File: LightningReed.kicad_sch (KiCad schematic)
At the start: 12 parts, among them P1 Conn_WallPlug

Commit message: PFC
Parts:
- added C10: 68uF, symbol Device:C_Polarized
- added C4: 10pF, symbol Device:C_Small
- added C5: 3900pF, symbol Device:C_Small
- added C6: 1uF, symbol Device:C_Small
- added C7: 33nF, symbol Device:C_Small
- added C8: 220pF, symbol Device:C_Small
- added C9: 2200pF, symbol Device:C_Small
- added Q1: NCE65T180D, symbol Device:Q_NMOS_GDS
- added R1: 10, symbol Device:R_Small
- added R10, R11, R12, R2, R3, R4: 3M24, symbol Device:R_Small
- added R13: 274K, symbol Device:R_Small
- added R14: 64k9, symbol Device:R_Small
- added R5: 24K3, symbol Device:R_Small
- added R6, R7: 220m, symbol Device:R_Small
- added R8: 182K, symbol Device:R_Small
- added R9: 750, symbol Device:R_Small
- added U1: UCC28056, symbol LightningReed:UCC28056
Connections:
- net GNDPWR: now also C10.2, C7.1, C8.2, C9.2, R14.1, R6.1, R7.1, R8.1, U1.4 (GND)
- net VDC: now also C10.1, R10.2
- net at D3.2 (A), L4.1: now also C4.1, Q1.2 (D), R2.2
- new net: R1.1, U1.5 (DRV)
- new net: Q1.1 (G), R1.2
- new net: R3.1, R4.2
- new net: R2.1, R3.2
- new net: C5.2, Q1.3 (S), R5.1, R6.2, R7.2
- new net: C4.2, C5.1, R4.1, R5.2, R9.1
- new net: R12.1, R13.2
- new net: R11.1, R12.2
- new net: C6.1, R8.2
- new net: C6.2, C7.2, U1.6 (COMP)
- new net: C9.1, R13.1, R14.2, U1.1 (VOSNS)
- new net: C8.1, R9.2, U1.2 (ZCD)
- new net: R10.1, R11.2
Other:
- note added: "EWH2WM680M20OT"

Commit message: brown out circuit
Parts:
- added C11, C12, C13: 1uF, symbol Device:C_Small
- added C14: 220pF, symbol Device:C_Small
- added Q2: 2N7002, Package_TO_SOT_SMD:SOT-23, symbol Transistor_FET:2N7002
- added R15: 2, symbol Device:R_Small
- added R16: 121K, symbol Device:R_Small
- added R17: 39K2, symbol Device:R_Small
- added R18: 100K, symbol Device:R_Small
- added U2: 78L05S, Package_TO_SOT_SMD:SOT-89-3, symbol Regulator_Linear:L78L05_SOT89
- added U3: LMC7111, symbol LightningReed:LMC7111
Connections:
- net GNDPWR: now also C11.2, C12.2, C13.2, C14.2, Q2.2 (S), R17.1, U2.2 (GND), U3.5 (V-)
- net at U1.3 (VCC): now also C11.1, R15.1
- new net: Q2.1 (G), R18.1, U3.1
- new net: R16.1, R17.2, R18.2, U3.3 (+)
- new net 5V_LDO: C13.1, R16.2, U2.1 (OUT), U3.2 (V+)
- new net AC_SENSE: C14.1, U3.4 (-)
- new net BROWN_OUT: Q2.3 (D)
- new net VCC_PFC: R15.2
- new net VDD3: C12.1, U2.3 (IN)

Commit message: PFC complete
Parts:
- added C15: 1uF, symbol Device:C_Small
- added C16, C18, C19, C20: 100nF, symbol Device:C_Small
- added C17: 33nF, symbol Device:C_Small
- added D4: BZT52C16S, symbol Device:D_Zener_Small
- added D5: DSK16, symbol Device:D_Schottky_Small
- added D6: BZT52C13, symbol Device:D_Zener_Small
- added Q3: Q_NMOS_GDS, symbol Device:Q_NMOS_GDS
- added Q4: 2N7002, Package_TO_SOT_SMD:SOT-23, symbol Transistor_FET:2N7002
- added Q5, Q6: 2N7002K, Package_TO_SOT_SMD:SOT-23, symbol Transistor_FET:2N7002K
- added R19, R20, R24: 3M24, symbol Device:R_Small
- added R21, R22, R23: 1K, symbol Device:R_Small
- added R25: 3M16, symbol Device:R_Small
- added R26: 178K, symbol Device:R_Small
- added R27, R28: 100K, symbol Device:R_Small
- added R29: 10K, symbol Device:R_Small
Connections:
- net AC_SENSE: now also R25.1, R26.2
- net BROWN_OUT: now also D4.1 (K), Q3.1 (G), Q4.1 (G), R24.1
- net GNDPWR: now also C15.2, C16.2, C17.2, C18.2, C19.2, C20.2, D4.2 (A), Q5.2 (S), Q6.2 (S), R26.1, R28.1, R29.1
- net HT: now also R19.2
- net VCC_PFC: now also C15.1, Q4.2 (S)
- net VDC: now also C18.1, C19.1, C20.1, R21.1
- net VDD3: now also D5.2 (A)
- net COMP: now reaches C6.2, C7.2, U1.6 (COMP)
- net COMP: now also Q5.3 (D)
- new net: D6.2 (A), Q6.1 (G), R29.2
- new net: D5.1 (K), Q3.3 (S), Q4.3 (D)
- new net: C16.1, R20.1, R24.2, R25.2
- new net: R22.2, R23.1
- new net: Q3.2 (D), R23.2
- new net: R21.2, R22.1
- new net: C17.1, Q5.1 (G), Q6.3 (D), R27.1, R28.2
- new net: R19.1, R20.2
- new net VDD2: D6.1 (K), R27.2

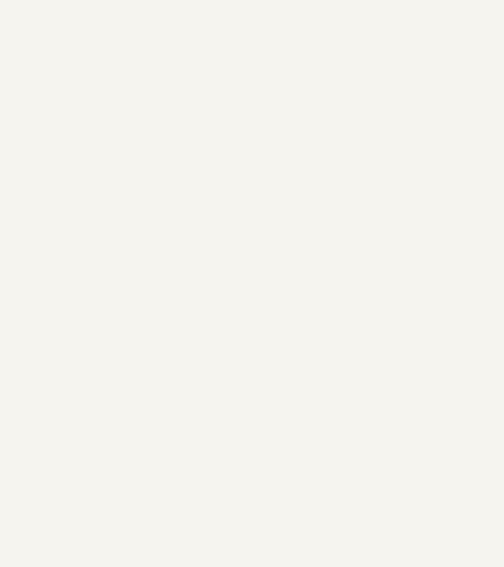
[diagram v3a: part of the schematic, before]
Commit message: Flyback controller
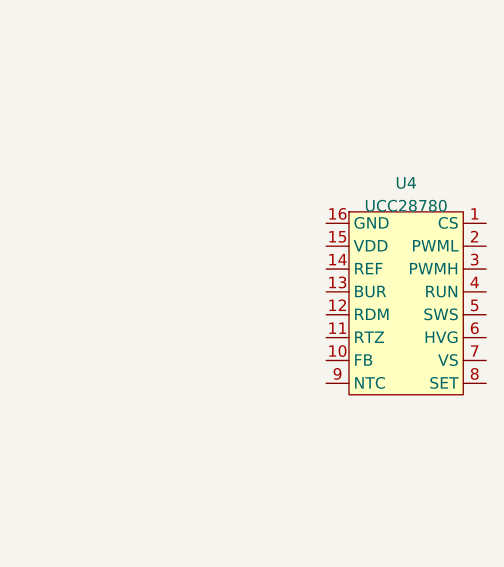
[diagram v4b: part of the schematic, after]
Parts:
- added U4: UCC28780, symbol LightningReed:UCC28780
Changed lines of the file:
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@@
+    )
+  )
+  (symbol (lib_id "LightningReed:UCC28780") (at 234.315 88.265 0) (unit 1)
+    (in_bom yes) (on_board yes) (dnp no) (fields_autoplaced)
+    (property "Reference" "U4" (at 234.315 85.09 0)
+      (effects (font (size 1.27 1.27)))
+    )
+    (property "Value" "UCC28780" (at 234.315 87.63 0)
+      (effects (font (size 1.27 1.27)))
+    )
+    (property "Footprint" "" (at 234.315 88.265 0)
+      (effects (font (size 1.27 1.27)) hide)
+    )
+    (property "Datasheet" "" (at 234.315 88.265 0)
+      (effects (font (size 1.27 1.27)) hide)
+    )
+    (pin "1")
+    (pin "10")
+    (pin "11")
+    (pin "12")
+    (pin "13")
+    (pin "14")
+    (pin "15")
+    (pin "16")
+    (pin "2")
+    (pin "3")
+    (pin "4")
+    (pin "5")
+    (pin "6")
+    (pin "7")
+    (pin "8")
+    (pin "9")
+    (instances
+      (project "LightningReed"
+        (path "/ed30a684-3009-4c45-ba04-268ec6465166"
+          (reference "U4") (unit 1)
+        )
+      )
     )
   )

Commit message: Transformer
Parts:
- added C21, C22: 330nF, symbol Device:C_Small
- added Q7, Q8: NCE65T260K, symbol Device:Q_NMOS_GDS
- added R30: 2M21, symbol Device:R_Small
- added T1: Transformer_2P_2S, symbol LightningReed:Transformer_2P_2S
- C19: value 100nF -> 470nF
- C20: value 100nF -> 330nF
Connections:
- net GNDPWR: no longer C20.2
- net VDC: now also C21.1, C22.1, R30.2, T1.2 (AB)
- new net: C20.2, C21.2, C22.2, Q7.2 (D), R30.1
- new net: Q7.3 (S), Q8.2 (D), T1.1 (AA)

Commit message: HB Driver
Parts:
- added C23: 47nF, symbol Device:C_Small
- added D7: ES1JAF, symbol Device:D_Schottky_Small
- added R31, R35: 10, symbol Device:R_Small
- added R32, R34: 10K, symbol Device:R_Small
- added R33: 24.9, symbol Device:R_Small
- added R36: 44K2, symbol Device:R_Small
- added R37: 118K, symbol Device:R_Small
- added U5: UCC27712, symbol LightningReed:UCC27712
- added U6: NCP1117-ADJ_SOT223, Package_TO_SOT_SMD:SOT-223-3_TabPin2, symbol Regulator_Linear:NCP1117-ADJ_SOT223
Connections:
- net at Q7.3 (S), Q8.2 (D), T1.1 (AA): now also C23.2, R32.2, U5.6 (HS)
- net at Q8.1 (G): now also R33.1, R34.1
- net at Q8.3 (S): now also R34.2, R37.2, U5.4 (COM)
- net at Q7.1 (G): now also R31.1, R32.1
- new net: C23.1, R35.1, U5.8 (HB)
- new net: R36.2, R37.1, U6.1 (ADJ)
- new net: D7.2 (A), R36.1, U5.3 (VDD), U6.2 (VO)
- new net: R33.2, U5.5 (LO)
- new net: R31.2, U5.7 (HO)
- new net: D7.1 (K), R35.2

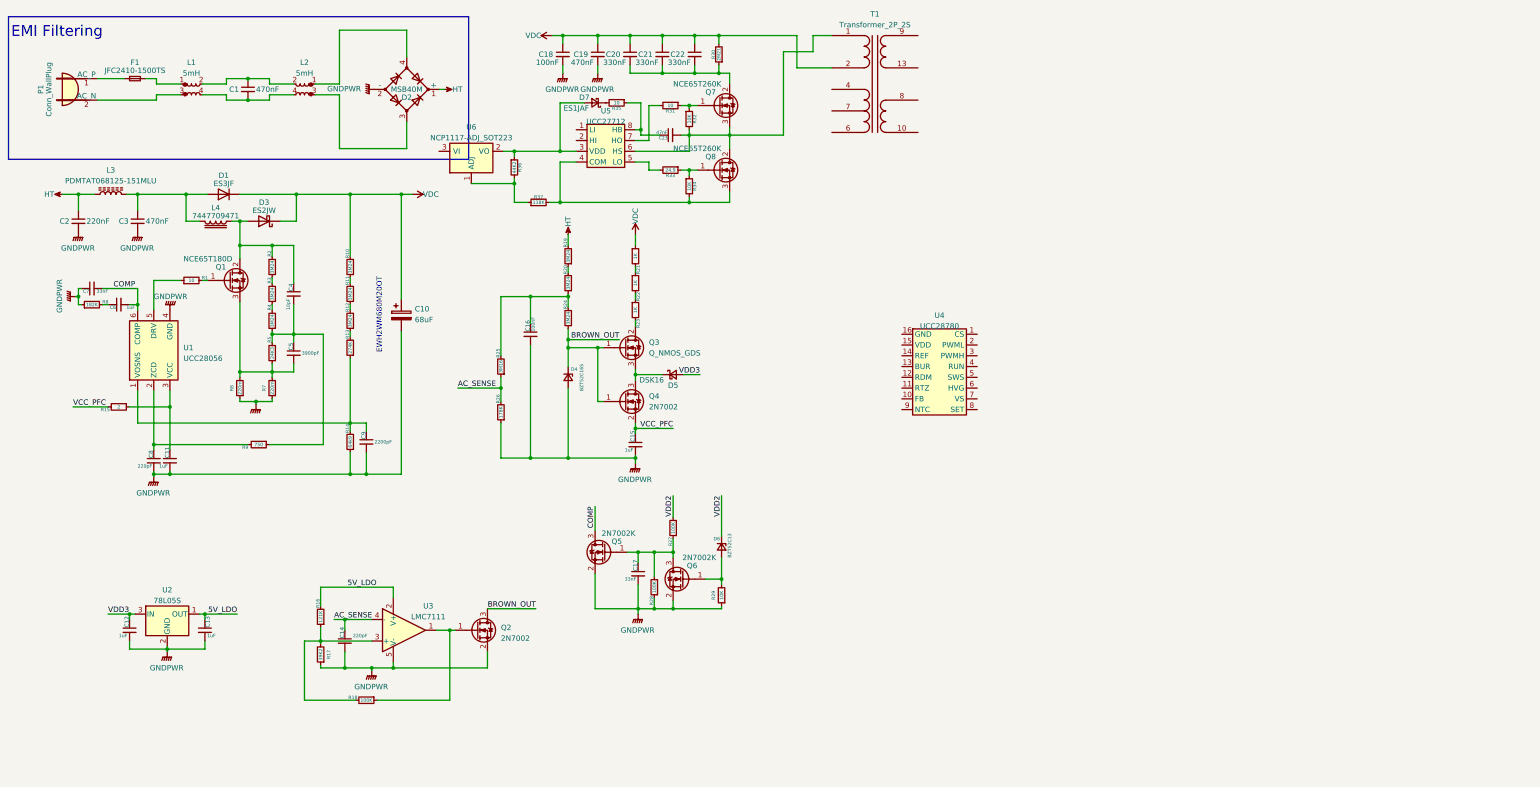
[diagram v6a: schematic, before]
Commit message: Flyback Controller VDDBias Power
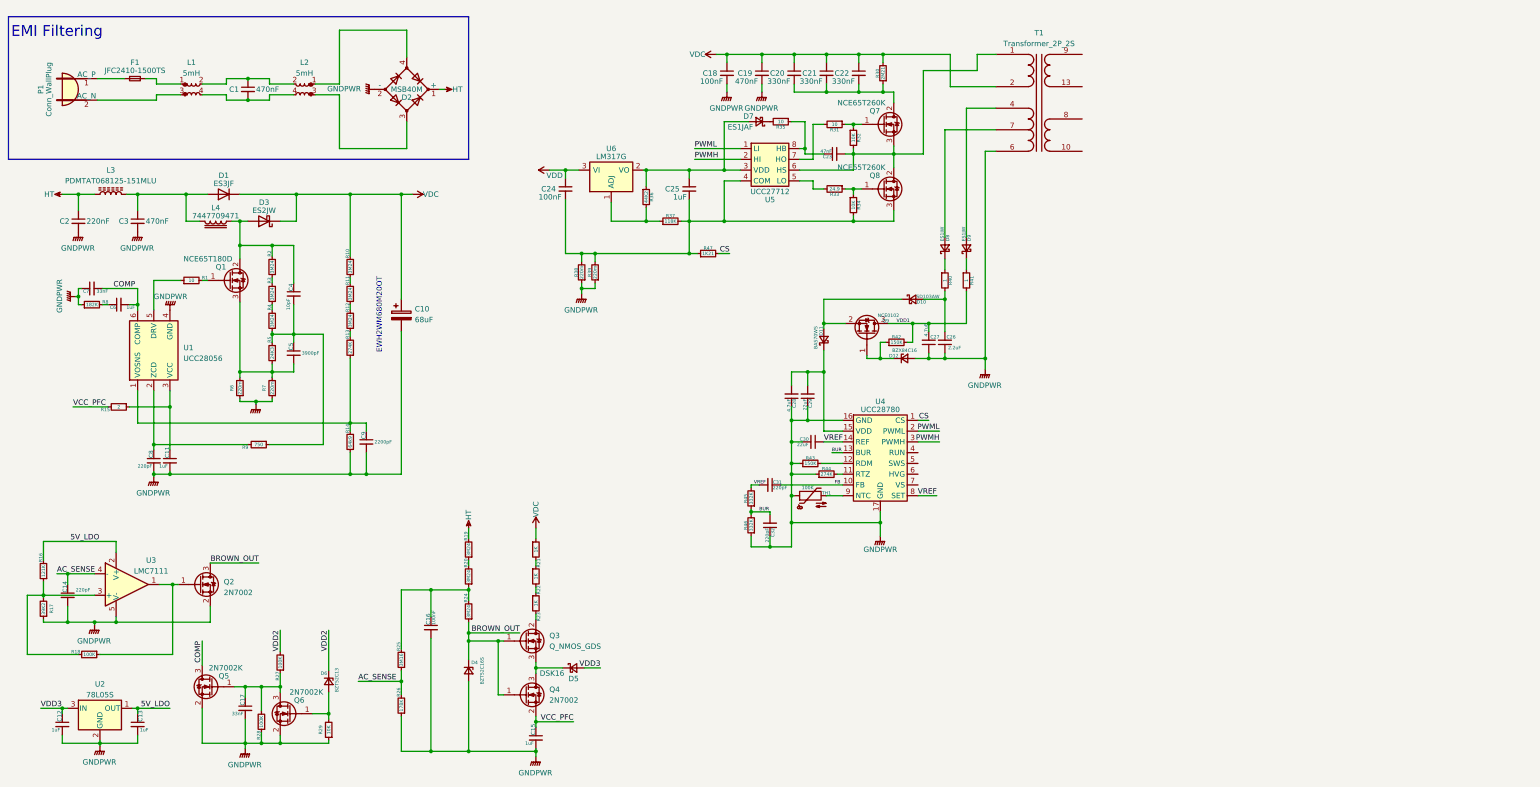
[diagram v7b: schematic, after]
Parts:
- added C24: 100nF, symbol Device:C_Small
- added C25: 1uF, symbol Device:C_Small
- added C26: 2.2uF, symbol Device:C_Small
- added C27, C28: 4.7uF, symbol Device:C_Small
- added C29, C30: 22uF, symbol Device:C_Small
- added C31, C32: 220pF, symbol Device:C_Small
- added D10: SD103AW, symbol Device:D_Schottky_Small
- added D11: BAS70WS, symbol Device:D_Schottky_Small
- added D12: BZX84C16, symbol Device:D_Zener_Small
- added D8, D9: ES1JW, symbol Device:D_Schottky_Small
- added Q9: NCE0102, symbol Device:Q_NMOS_GSD
- added R38, R39: 220m, symbol Device:R_Small
- added R40, R41: 1, symbol Device:R_Small
- added R42, R43: 150K, symbol Device:R_Small
- added R44: 274K, symbol Device:R_Small
- added R45, R46: 332K, symbol Device:R_Small
- added R47: 1K21, symbol Device:R_Small
- added TH1: 100K, symbol Device:Thermistor_NTC
- U6: value NCP1117-ADJ_SOT223 -> LM317G
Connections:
- net GNDPWR: now also T1.6 (SD), U4.16 (GND), U4.17 (GND), C26.1, C27.1, C28.1, C29.1, C30.2, C32.1, D12.2 (A), R38.1, R39.1, R43.1, R44.1, R46.1, TH1.1
- net CS: now reaches U4.1 (CS)
- net CS: now also R47.2
- net FB: now reaches U4.10 (FB)
- net FB: now also C31.1
- net at U4.11 (RTZ): now also R44.2
- net at U4.12 (RDM): now also R43.2
- net BUR: now reaches U4.13 (BUR)
- net BUR: now also C32.2, R45.1, R46.2
- net VREF: now reaches U4.14 (REF)
- net VREF: now also U4.8 (SET), C30.1, C31.2, R45.2
- net at U4.15 (VDD): now also C28.2, C29.2, D11.1 (K)
- net PWML: now reaches U4.2 (PWML)
- net PWML: now also U5.1 (LI)
- net PWMH: now reaches U4.3 (PWMH)
- net PWMH: now also U5.2 (HI)
- net at U4.9 (NTC): now also TH1.2
- net at Q8.3 (S), R34.2, R37.2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: now also C24.2, C25.2, R38.2, R39.2, R47.1
- net at D7.2 (A), R36.1, U5.3 (VDD)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: now also C25.1
- net at T1.4 (SC): now also D9.2 (A)
- net at T1.7 (SD): now also D8.2 (A)
- net VDD: now reaches U6.3 (VI)
- net VDD: now also C24.1
- new net: D9.1 (K), R41.1
- new net: D8.1 (K), R40.1
- new net: C26.2, D10.2 (A), R40.2
- new net: D12.1 (K), Q9.1 (G), R42.1
- new net: D10.1 (K), D11.2 (A), Q9.2 (S)
- new net VDD1: C27.2, Q9.3 (D), R41.2, R42.2
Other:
- moved on the sheet: C12, C13, C14, C15, C16, C17, C18, C19, C20, C21, C22, C23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

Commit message: Complete Schematic
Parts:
- added C33: 33pF, symbol Device:C_Small
- added C34: 22pF, symbol Device:C_Small
- added C35: 4.7nF, symbol Device:C_Small
- added C36: 10nF, symbol Device:C_Small
- added C37: 3.3pF, symbol Device:C_Small
- added C38: 220pF, symbol Device:C_Small
- added C39, C40, C41, C42: 33uF, symbol Device:C_Small
- added C43: 680uF, symbol Device:C_Small
- added C44, C45, C46: 1uF, symbol Device:C_Small
- added C47: 2.2uF, symbol Device:C_Small
- added D13: MM3Z20, symbol Device:D_Zener_Small
- added D14: MM3Z24, symbol Device:D_Zener_Small
- added D15: RF081M2STR, symbol Device:D_Small
- added D16: MM3Z10, symbol Device:D_Zener_Small
- added D17: RFU02VSM8S, symbol Device:D_Schottky_Small
- added L5: 1uH, symbol Device:L_Iron
- added L6: 680nH, symbol Device:L_Iron
- added Q10: DMZ6005E, symbol Device:Q_NMOS_GDS
- added Q11: 2N7002K, Package_TO_SOT_SMD:SOT-23, symbol Transistor_FET:2N7002K
- added Q12: NCEP15T14D, Package_TO_SOT_SMD:LFPAK33, symbol Device:Q_NMOS_GDS
- added Q13: BSS123, Package_TO_SOT_SMD:SOT-23, symbol Transistor_FET:BSS123
- added R48: 1M, symbol Device:R_Small
- added R49: 121, symbol Device:R_Small
- added R50: 12K4, symbol Device:R_Small
- added R51, R63: 75K, symbol Device:R_Small
- added R52: 30K1, symbol Device:R_Small
- added R53: 432K, symbol Device:R_Small
- added R54: 10, symbol Device:R_Small
- added R55: 562, symbol Device:R_Small
- added R56, R57: 10K, symbol Device:R_Small
- added R58, R60: 150K, symbol Device:R_Small
- added R59: 56K2, symbol Device:R_Small
- added R61: 22, symbol Device:R_Small
- added R62: 100, symbol Device:R_Small
- added TP1, TP2, TP3, TP4: TestPoint_Alt, symbol Connector:TestPoint_Alt
- added U7: FODM8801A, Package_SO:SOP-4_4.4x2.6mm_P1.27mm, symbol Isolator:FODM217A
- added U8: TL431DBZ, Package_TO_SOT_SMD:SOT-23, symbol Reference_Voltage:TL431DBZ
- added U9: UCC24612-1DBV, Package_TO_SOT_SMD:SOT-23-5, symbol Regulator_Controller:UCC24612-1DBV
- C1, C2: footprint (none) -> LightningReed:C_Rect_L10.0mm_W6.0mm_P7.50mm_MKS4
- C10: footprint (none) -> Capacitor_THT:CP_Radial_D18.0mm_P7.50mm
- C30: value 22uF -> 100nF
- C4: footprint (none) -> Capacitor_SMD:C_0805_2012Metric
- C5, C6, C7, C8, C9: footprint (none) -> Capacitor_SMD:C_0603_1608Metric
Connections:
- net CS: now also C33.2
- net GNDPWR: now also C33.1, C34.2, D13.2 (A), D14.2 (A), Q11.2 (S), R50.1, U7.3
- net VDD2: now also C26.2, D10.2 (A), R40.2
- net VDD3: now also D10.1 (K), D11.2 (A), Q9.2 (S)
- net RUN: now reaches U4.4 (RUN)
- net RUN: now also Q11.1 (G)
- net at U4.5 (SWS): now also C34.1, D13.1 (K), R48.1, R49.1
- net at U4.6 (HVG): now also D14.1 (K), Q10.1 (G), R48.2
- net at U4.7 (VS): now also R50.2, R51.2
- net VSW: now reaches C23.2, Q7.3 (S), Q8.2 (D), R32.2, T1.1 (AA), U5.6 (HS)
- net VSW: now also Q10.2 (D)
- net VS: now reaches T1.10 (SD)
- net VS: now also C44.1, C45.1, C46.2, C47.1, D16.2 (A)
- net GNDS: now reaches T1.13 (SB)
- net GNDS: now also C39.2, C40.2, C41.2, C42.2, C43.2, R60.1, TP3.1, U8.3 (A)
- net VSV: now reaches D8.2 (A), T1.7 (SD)
- net VSV: now also R51.1
- net VAUX: now reaches T1.8 (SC)
- net VAUX: now also D15.2 (A)
- net at T1.9 (SA): now also C38.1, Q12.3 (S), U9.2 (VS)
- new net: Q10.3 (S), R49.2
- new net: C44.2, D15.1 (K), Q13.3 (D), R63.2
- new net: C36.1, R59.1
- new net: C37.1, R57.1, R59.2, U7.2, U8.1 (K)
- new net: D16.1 (K), Q13.1 (G), R63.1
- new net: Q11.3 (D), R53.2
- new net: R54.1, R55.2, R56.2, R58.2
- new net: C45.2, C46.1, D17.1 (K), Q13.2 (S), U9.4 (VDD)
- new net: C35.2, R56.1, R57.2, U7.1
- new net: R52.1, U7.4
- new net: R52.2, R53.1
- new net: Q12.1 (G), U9.1 (VG)
- new net: C47.2, U9.3 (REG)
- new net: R62.2, U9.5 (VD)
- new net: C38.2, R61.2
- new net: C35.1, R55.1
- new net CTL: C36.2, C37.2, R58.1, R60.2, TP4.1, U8.2 (REF)
- new net LINE: C43.1, D17.2 (A), L5.2, L6.2, R54.2, TP1.1
- new net VCOM: C39.1, C40.1, C41.1, C42.1, L5.1, L6.1, Q12.2 (D), R61.1, R62.1, TP2.1
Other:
- moved on the sheet: D10
